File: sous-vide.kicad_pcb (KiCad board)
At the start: 2 copper layers, 100 x 70 mm, 31 parts, among them J1 Heater, J2 Power, J3 Conn_01x02, J4 Jumper, J5 Jumper, Q1 2N3904, SW1 SW_Push_Dual, SW2 SW_Push_Dual, U1 G5LE, U2 RAC01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

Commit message: added all pin labels to nodemcu footprint
 - add helpful labels on back
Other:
- board text added: "A0"
- board text added: "BLUE_LED"
- board text added: "CLK"
- board text added: "DAT"
- board text added: "RED_LED"
- board text added: "Relay"
- board text added: "SW1"
- board text added: "SW2"
- board text added: "THERMISTOR"
- board text added: "USER_POT"
- board text added: "VIN"

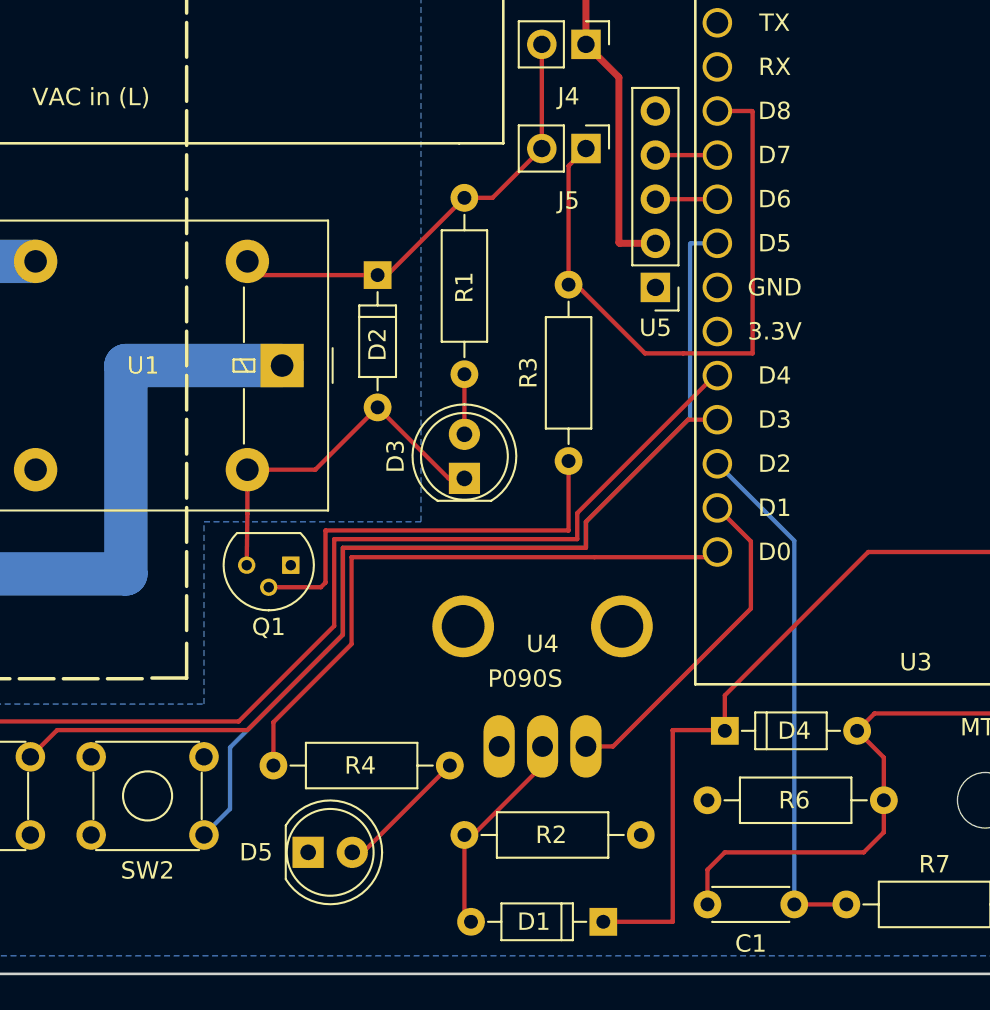
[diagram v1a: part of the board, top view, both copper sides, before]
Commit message: rerouted wires so there are no breaks in the ground plane
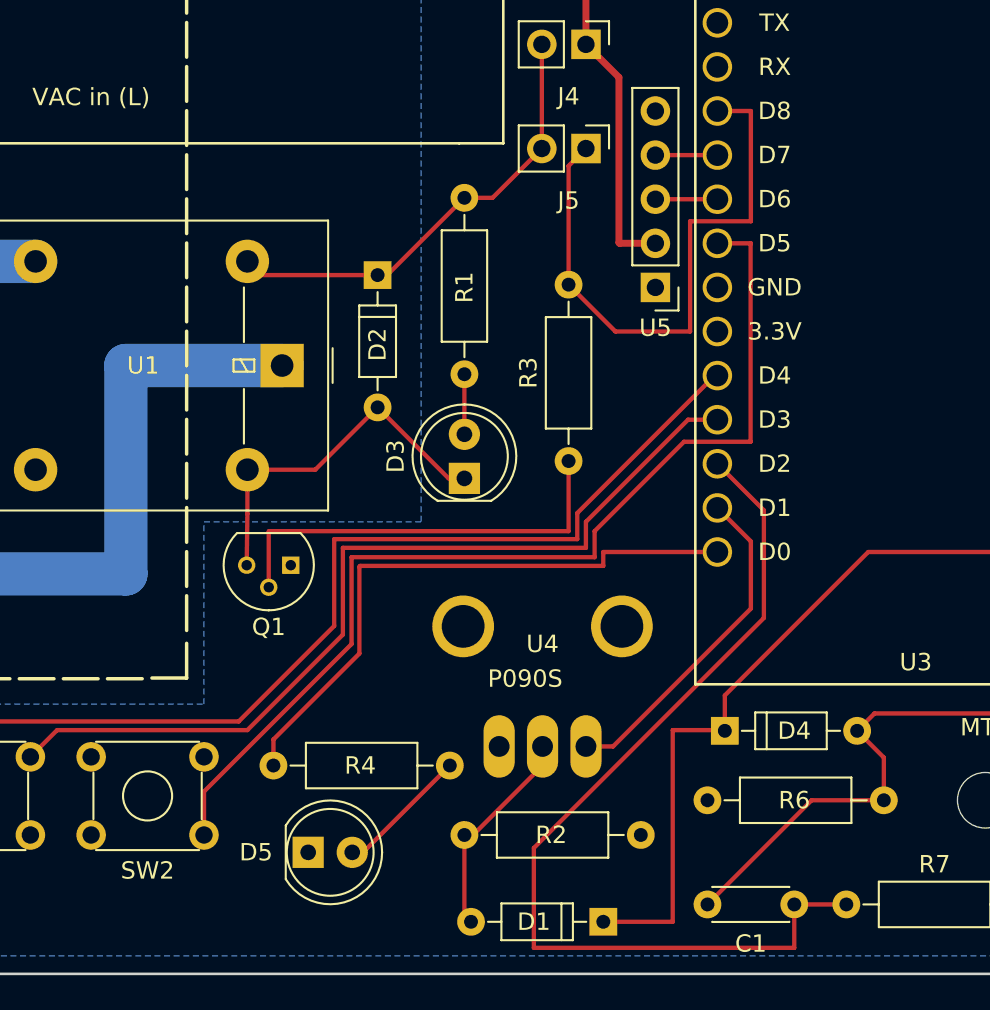
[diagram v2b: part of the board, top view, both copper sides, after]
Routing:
- net /THERMISTOR: track 30.2 -> 55.0 mm
- net /SW2: track 55.4 -> 59.5 mm
- net Net-(C1-Pad2): track 35.7 -> 33.5 mm
- net /Relay: track 36.7 -> 34.5 mm
- net /-coil: track 21.9 -> 21.2 mm
